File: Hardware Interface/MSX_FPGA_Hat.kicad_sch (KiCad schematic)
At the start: 31 parts, among them J1 J1, J2 J2, J3a1 J3a, J3b1 J3b, J4a1 J4a, J4b1 J4b, J5 Conn_01x03_Female, U1 74LVC245A, U2 74LVC245A, U3 74LVC245A, U4 74LVC245A, U5 74LVC245A, U6 LM1117-3.3

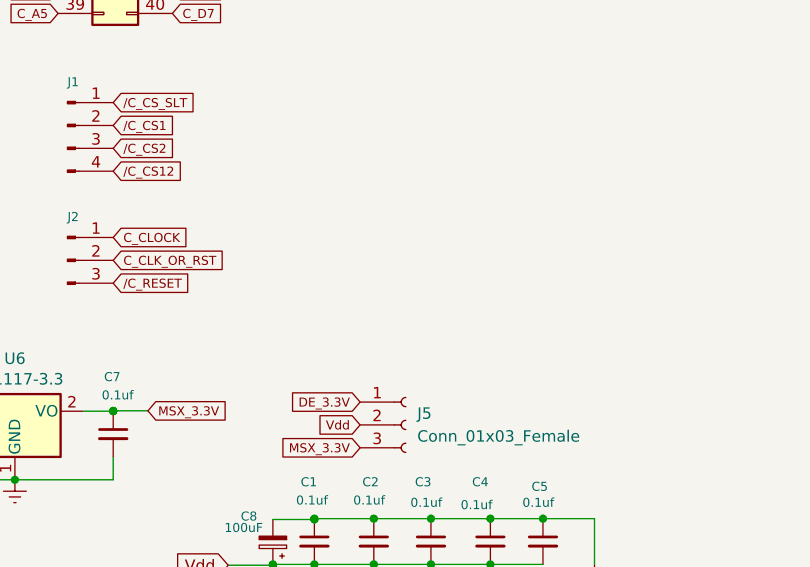
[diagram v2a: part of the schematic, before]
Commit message: Added pull-ups for int,wait,busdir (optional)
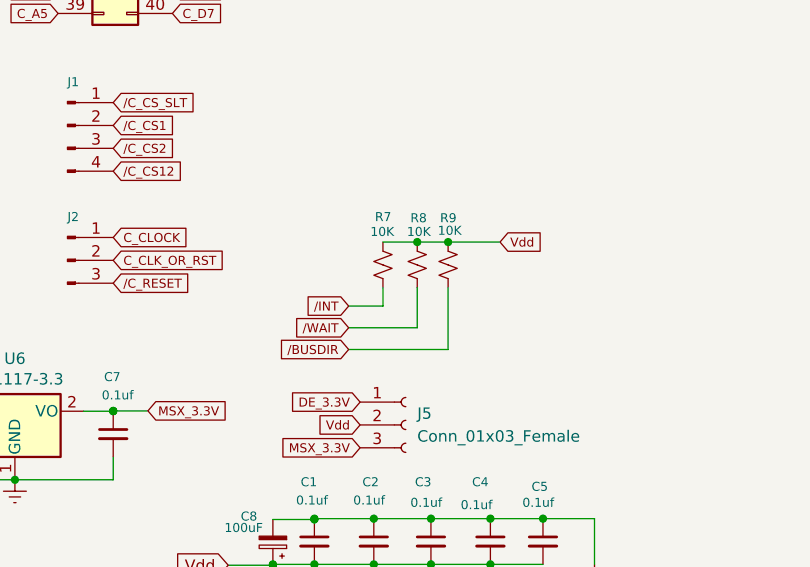
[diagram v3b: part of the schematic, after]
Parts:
- added R7, R8, R9: 10K, Resistor_THT:R_Axial_DIN0207_L6.3mm_D2.5mm_P7.62mm_Horizontal, symbol Device:R_Small_US
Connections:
- net Vdd: now also R7.1, R8.1, R9.1
- net /BUSDIR: now also R9.2
- net /INT: now also R7.2
- net /WAIT: now also R8.2
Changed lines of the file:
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@@
   (junction (at 73.279 46.863) (diameter 0) (color 0 0 0 0)
   )
+  (junction (at 172.339 119.38) (diameter 0) (color 0 0 0 0)
+  )
   (junction (at 90.424 61.849) (diameter 0) (color 0 0 0 0)
   )
@@
   )
   (junction (at 73.279 86.36) (diameter 0) (color 0 0 0 0)
+  )
+  (junction (at 168.91 119.38) (diameter 0) (color 0 0 0 0)
   )
   (junction (at 182.88 150.114) (diameter 0) (color 0 0 0 0)
@@
     (stroke (width 0) (type default) (color 0 0 0 0))
   )
+  (wire (pts (xy 168.91 119.38) (xy 172.339 119.38))
+    (stroke (width 0) (type default) (color 0 0 0 0))
+  )
   (wire (pts (xy 47.6509 90.805) (xy 47.6509 151.511))
     (stroke (width 0) (type default) (color 0 0 0 0))
@@
     (stroke (width 0) (type default) (color 0 0 0 0))
   )
+  (wire (pts (xy 172.339 119.38) (xy 178.1084 119.38))
+    (stroke (width 0) (type default) (color 0 0 0 0))
+  )
+  (wire (pts (xy 165.1 126.492) (xy 165.1 124.46))
+    (stroke (width 0) (type default) (color 0 0 0 0))
+  )
   (wire (pts (xy 30.353 177.165) (xy 46.228 177.165))
     (stroke (width 0) (type default) (color 0 0 0 0))
@@
     (stroke (width 0) (type default) (color 0 0 0 0))
   )
+  (wire (pts (xy 168.91 128.905) (xy 168.91 124.46))
+    (stroke (width 0) (type default) (color 0 0 0 0))
+  )
   (wire (pts (xy 30.353 167.005) (xy 33.1542 167.005))
     (stroke (width 0) (type default) (color 0 0 0 0))
@@
     (stroke (width 0) (type default) (color 0 0 0 0))
   )
+  (wire (pts (xy 161.29 126.492) (xy 165.1 126.492))
+    (stroke (width 0) (type default) (color 0 0 0 0))
+  )
   (wire (pts (xy 41.148 169.545) (xy 46.228 169.545))
     (stroke (width 0) (type default) (color 0 0 0 0))
@@
     (stroke (width 0) (type default) (color 0 0 0 0))
   )
+  (wire (pts (xy 161.29 131.318) (xy 172.339 131.318))
+    (stroke (width 0) (type default) (color 0 0 0 0))
+  )
   (wire (pts (xy 92.178 61.8336) (xy 90.424 61.8336))
     (stroke (width 0) (type default) (color 0 0 0 0))
   )
+  (wire (pts (xy 161.29 128.905) (xy 168.91 128.905))
+    (stroke (width 0) (type default) (color 0 0 0 0))
+  )
+  (wire (pts (xy 165.1 119.38) (xy 168.91 119.38))
+    (stroke (width 0) (type default) (color 0 0 0 0))
+  )
   (wire (pts (xy 30.353 169.545) (xy 41.148 169.545))
     (stroke (width 0) (type default) (color 0 0 0 0))
@@
   )
   (wire (pts (xy 170.434 155.194) (xy 177.038 155.194))
+    (stroke (width 0) (type default) (color 0 0 0 0))
+  )
+  (wire (pts (xy 172.339 131.318) (xy 172.339 124.46))
     (stroke (width 0) (type default) (color 0 0 0 0))
   )
@@
     )
   )
+  (global_label "Vdd" (shape input) (at 178.1084 119.38 0) (fields_autoplaced)
+    (effects (font (size 1 1)) (justify left))
+    (property "Intersheet References" "${INTERSHEET_REFS}" (id 0) (at 183.9082 119.3006 0)
+      (effects (font (size 1 1)) (justify left) hide)
+    )
+  )
   (global_label "C_A4" (shape input) (at 129.0044 91.44 180) (fields_autoplaced)
     (effects (font (size 1 1)) (justify right))
@@
     )
   )
+  (global_label "{slash}INT" (shape input) (at 161.29 126.492 180) (fields_autoplaced)
+    (effects (font (size 1 1)) (justify right))
+    (property "Intersheet References" "${INTERSHEET_REFS}" (id 0) (at 154.6436 126.5714 0)
+      (effects (font (size 1 1)) (justify right) hide)
+    )
+  )
   (global_label "D0" (shape input) (at 73.406 228.092 180) (fields_autoplaced)
     (effects (font (size 1.27 1.27)) (justify right))
@@
     )
   )
+  (global_label "{slash}BUSDIR" (shape input) (at 161.29 131.318 180) (fields_autoplaced)
+    (effects (font (size 1 1)) (justify right))
+    (property "Intersheet References" "${INTERSHEET_REFS}" (id 0) (at 150.5917 131.3974 0)
+      (effects (font (size 1 1)) (justify right) hide)
+    )
+  )
   (global_label "C_D1" (shape input) (at 90.678 225.806 0) (fields_autoplaced)
     (effects (font (size 1 1)) (justify left))
@@
     (property "Intersheet References" "${INTERSHEET_REFS}" (id 0) (at 94.254 175.8513 0)
       (effects (font (size 1 1)) (justify left) hide)
+    )
+  )
+  (global_label "{slash}WAIT" (shape input) (at 161.29 128.905 180) (fields_autoplaced)
+    (effects (font (size 1 1)) (justify right))
+    (property "Intersheet References" "${INTERSHEET_REFS}" (id 0) (at 155.1043 128.9675 0)
+      (effects (font (size 1 1)) (justify right) hide)
     )
   )
@@
     )
     (property "Datasheet" "~" (id 3) (at 92.2788 201.8607 0)
+      (effects (font (size 1 1)) hide)
+    )
+    (pin "1")
+    (pin "2")
+  )
+  (symbol (lib_id "Device:R_Small_US") (at 165.1 121.92 0) (unit 1)
+    (in_bom yes) (on_board yes)
+    (property "Reference" "R7" (id 0) (at 164.211 116.586 0)
+      (effects (font (size 1 1)) (justify left))
+    )
+    (property "Value" "10K" (id 1) (at 163.703 118.237 0)
+      (effects (font (size 1 1)) (justify left))
+    )
+    (property "Footprint" "Resistor_THT:R_Axial_DIN0207_L6.3mm_D2.5mm_P7.62mm_Horizontal" (id 2) (at 165.1 121.92 0)
+      (effects (font (size 1 1)) hide)
+    )
+    (property "Datasheet" "~" (id 3) (at 165.1 121.92 0)
       (effects (font (size 1 1)) hide)
     )
@@
     (pin "2")
   )
+  (symbol (lib_id "Device:R_Small_US") (at 168.91 121.92 0) (unit 1)
+    (in_bom yes) (on_board yes)
+    (property "Reference" "R8" (id 0) (at 168.148 116.713 0)
+      (effects (font (size 1 1)) (justify left))
+    )
+    (property "Value" "10K" (id 1) (at 167.767 118.237 0)
+      (effects (font (size 1 1)) (justify left))
+    )
+    (property "Footprint" "Resistor_THT:R_Axial_DIN0207_L6.3mm_D2.5mm_P7.62mm_Horizontal" (id 2) (at 168.91 121.92 0)
+      (effects (font (size 1 1)) hide)
+    )
+    (property "Datasheet" "~" (id 3) (at 168.91 121.92 0)
+      (effects (font (size 1 1)) hide)
+    )
+    (pin "1")
+    (pin "2")
+  )
+  (symbol (lib_id "Device:R_Small_US") (at 172.339 121.92 0) (unit 1)
+    (in_bom yes) (on_board yes)
+    (property "Reference" "R9" (id 0) (at 171.45 116.713 0)
+      (effects (font (size 1 1)) (justify left))
+    )
+    (property "Value" "10K" (id 1) (at 171.196 118.11 0)
+      (effects (font (size 1 1)) (justify left))
+    )
+    (property "Footprint" "Resistor_THT:R_Axial_DIN0207_L6.3mm_D2.5mm_P7.62mm_Horizontal" (id 2) (at 172.339 121.92 0)
+      (effects (font (size 1 1)) hide)
+    )
+    (property "Datasheet" "~" (id 3) (at 172.339 121.92 0)
+      (effects (font (size 1 1)) hide)
+    )
+    (pin "1")
+    (pin "2")
+  )
   (symbol (lib_id "Connector_Generic:Conn_02x01") (at 64.3266 61.5421 0) (unit 1)
     (in_bom yes) (on_board yes)
@@
       (reference "R6") (unit 1) (value "10K") (footprint "Resistor_THT:R_Axial_DIN0207_L6.3mm_D2.5mm_P7.62mm_Horizontal")
     )
+    (path "/456853ee-9e2f-47f8-8ca8-535879242fe0"
+      (reference "R7") (unit 1) (value "10K") (footprint "Resistor_THT:R_Axial_DIN0207_L6.3mm_D2.5mm_P7.62mm_Horizontal")
+    )
+    (path "/ea7a7743-f2cc-4532-baa8-31f11cef6d41"
+      (reference "R8") (unit 1) (value "10K") (footprint "Resistor_THT:R_Axial_DIN0207_L6.3mm_D2.5mm_P7.62mm_Horizontal")
+    )
+    (path "/ec470464-8761-4e29-aaed-1c482de3b5f5"
+      (reference "R9") (unit 1) (value "10K") (footprint "Resistor_THT:R_Axial_DIN0207_L6.3mm_D2.5mm_P7.62mm_Horizontal")
+    )
     (path "/b84ee47f-62a9-4217-a7bc-a9e806626d6a"

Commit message: Updated edge connector to meet MSX specifications
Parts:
- CONN1: footprint Roni Footprints:MSX_CART_SW -> Roni Footprints:MSX_CART_SW_Official
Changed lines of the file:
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@@
     (property "Reference" "CONN1" (id 0) (at 26.67 51.689 0))
     (property "Value" "MSX_BUS" (id 1) (at 26.924 53.721 0))
-    (property "Footprint" "Roni Footprints:MSX_CART_SW" (id 2) (at 98.298 146.177 0)
+    (property "Footprint" "Roni Footprints:MSX_CART_SW_Official" (id 2) (at 98.298 146.177 0)
       (effects (font (size 1 1)) hide)
     )
@@
     )
     (path "/a665c02f-f334-4e4d-81d4-866e92328b25"
-      (reference "CONN1") (unit 1) (value "MSX_BUS") (footprint "Roni Footprints:MSX_CART_SW")
+      (reference "CONN1") (unit 1) (value "MSX_BUS") (footprint "Roni Footprints:MSX_CART_SW_Official")
     )
     (path "/79659c5e-ee34-4dee-880c-5f7faad77490"

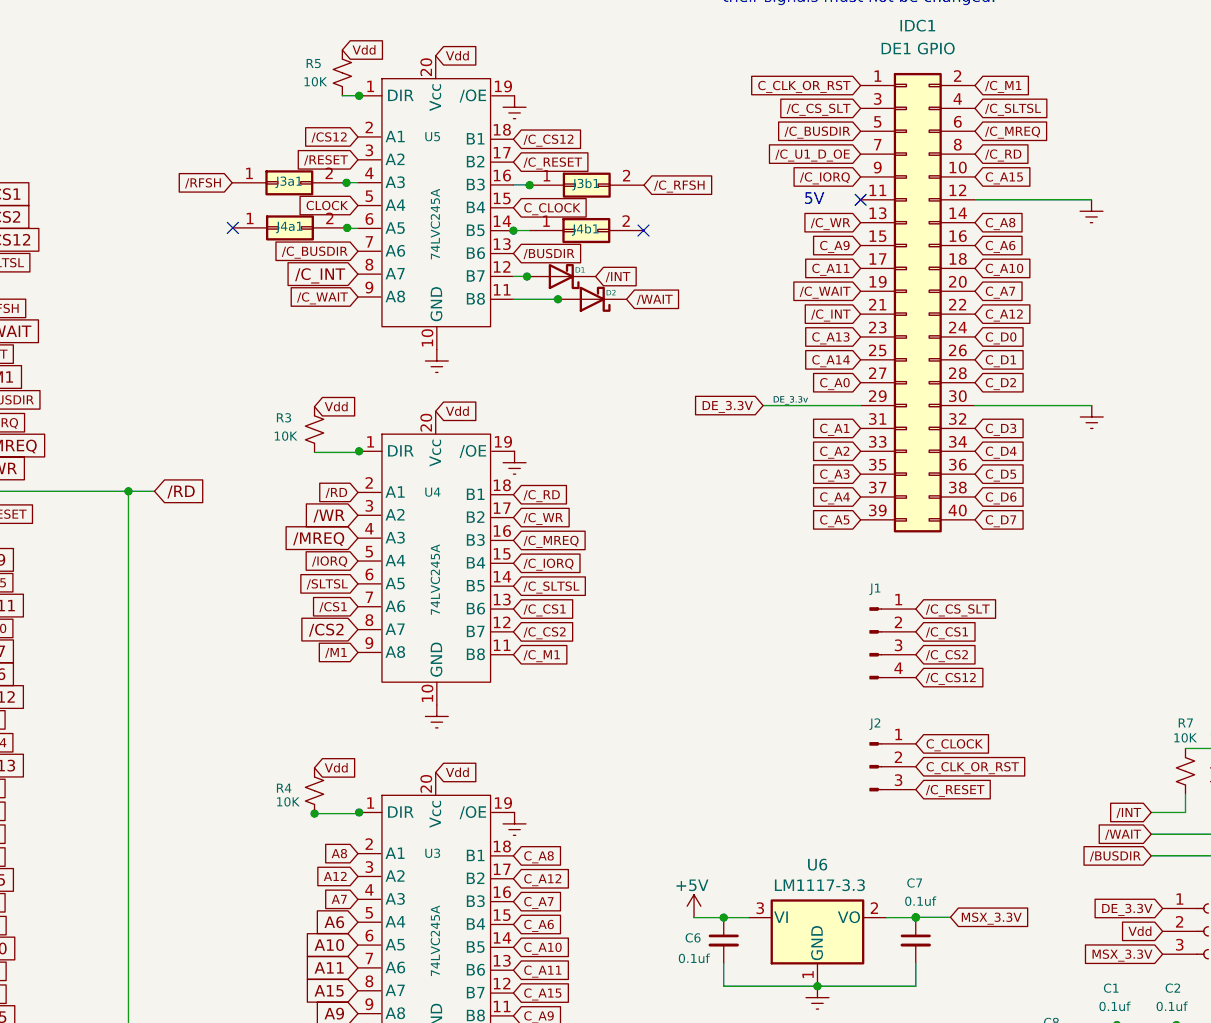
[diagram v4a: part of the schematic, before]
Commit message: Finalized v1.3; new silk; new routing for soundin & rfsh; changed jumper J1
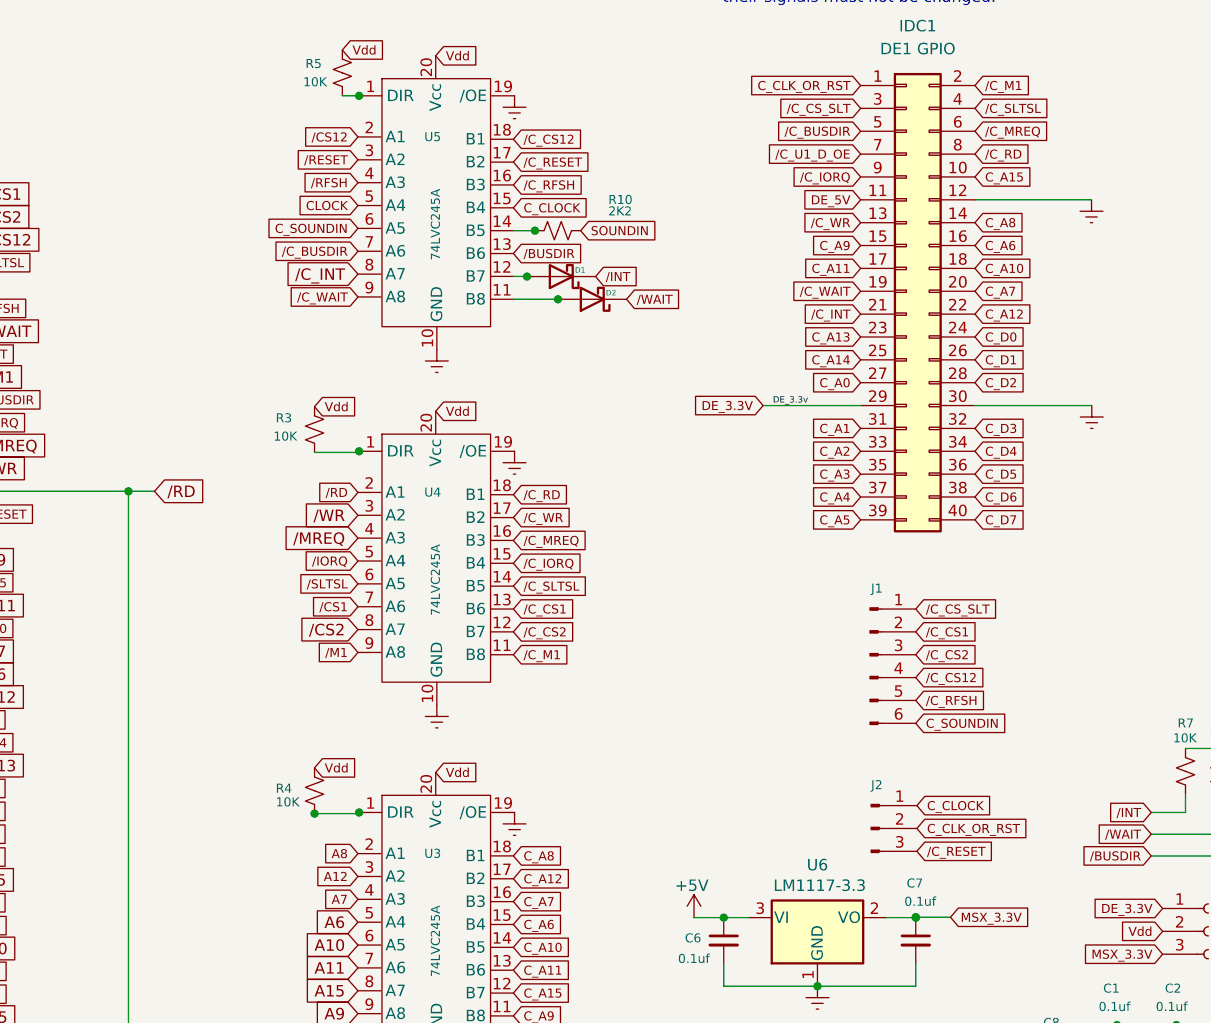
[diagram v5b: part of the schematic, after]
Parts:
- removed J3a1: J3a, Connector_PinHeader_2.54mm:PinHeader_1x02_P2.54mm_Vertical, symbol Connector_Generic:Conn_02x01
- removed J3b1: J3b, Connector_PinHeader_2.54mm:PinHeader_1x02_P2.54mm_Vertical, symbol Connector_Generic:Conn_02x01
- removed J4a1: J4a, Connector_PinHeader_2.54mm:PinHeader_1x02_P2.54mm_Vertical, symbol Connector_Generic:Conn_02x01
- removed J4b1: J4b, Connector_PinHeader_2.54mm:PinHeader_1x02_P2.54mm_Vertical, symbol Connector_Generic:Conn_02x01
- added R10: 2K2, Resistor_THT:R_Axial_DIN0207_L6.3mm_D2.5mm_P7.62mm_Horizontal, symbol Device:R_Small_US
- J1: footprint Connector_PinHeader_2.54mm:PinHeader_2x02_P2.54mm_Vertical -> Connector_PinHeader_2.54mm:PinHeader_2x03_P2.54mm_Vertical; symbol Connector:Conn_01x04_Male -> Connector:Conn_01x06_Male
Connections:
- net SOUNDIN: now also R10.1
- net /C_RFSH: now also J1.5 (Pin_5), U5.16 (B3)
- net /RFSH: now also U5.4 (A3)
- net DE_5V: now reaches IDC1.11 (Pin_11)
- net at U5.14 (B5): now also R10.2
- net C_SOUNDIN: now reaches U5.6 (A5)
- net C_SOUNDIN: now also J1.6 (Pin_6)
- no-connect marks 5 -> 2
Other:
- note removed: "5V"
- moved on the sheet: J2
